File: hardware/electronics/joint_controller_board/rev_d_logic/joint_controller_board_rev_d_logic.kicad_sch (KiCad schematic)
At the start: 43 parts, among them J1 J_IFACE, J2 J_ENCODERS, U1 Pico, U4 SN74LVC2G08, Y1 8MHz, Y2 8MHz

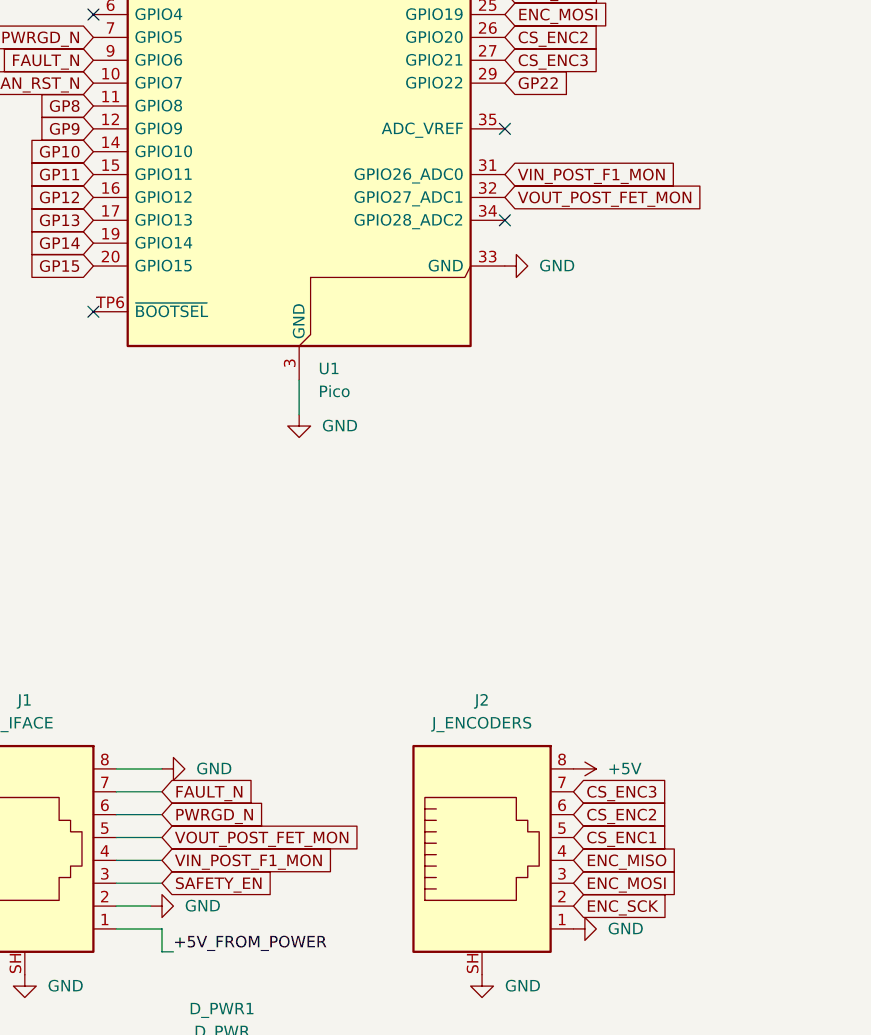
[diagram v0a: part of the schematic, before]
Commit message: hardware: align rev d logic raw monitor net
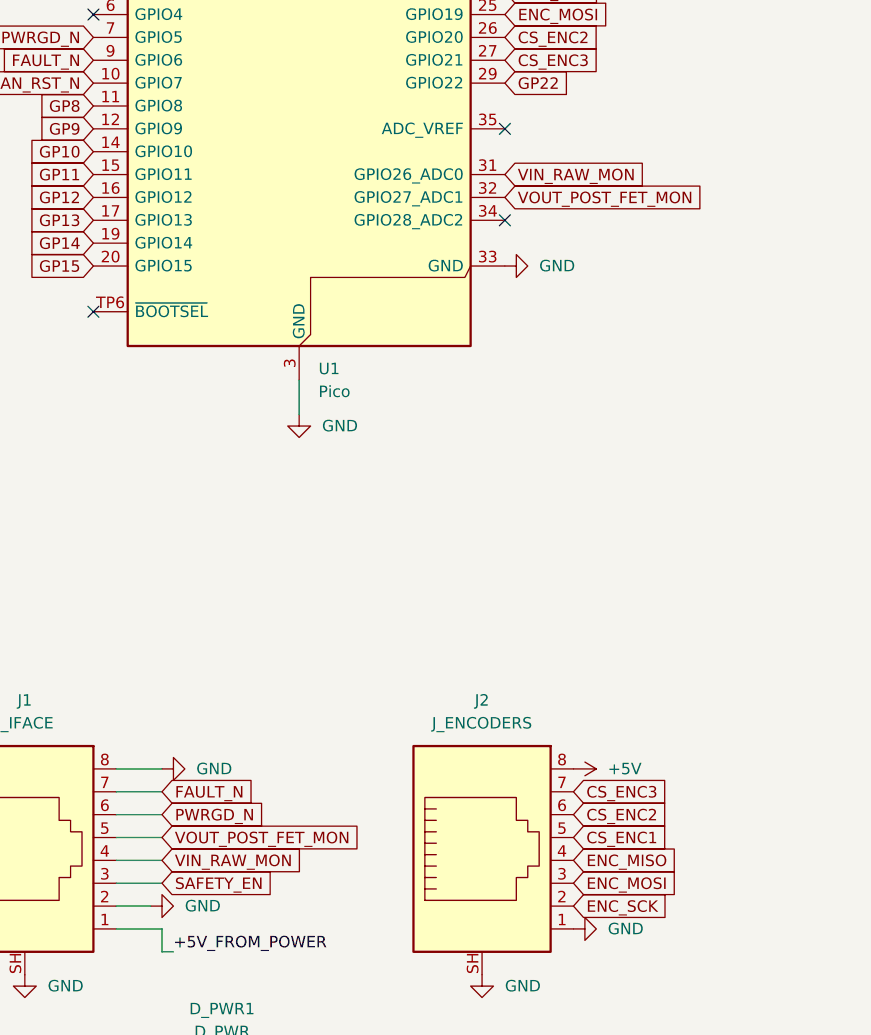
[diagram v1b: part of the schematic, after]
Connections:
- net VIN_POST_F1_MON renamed VIN_RAW_MON
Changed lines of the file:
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@@
 		)
 	)
-	(global_label "VIN_POST_F1_MON"
+	(global_label "VIN_RAW_MON"
 		(shape input)
 		(at 346.71 124.46 0)
@@
 		)
 	)
-	(global_label "VIN_POST_F1_MON"
+	(global_label "VIN_RAW_MON"
 		(shape input)
 		(at 308.61 200.66 0)
